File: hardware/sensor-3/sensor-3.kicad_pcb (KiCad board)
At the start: 2 copper layers, 11 x 32 mm, 12 parts, among them J101 2x05_Horizontal, U101 A31010SEHALT-10

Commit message: Update sensors
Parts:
- C101: footprint Capacitor_SMD:C_0603_1608Metric -> V2_Capacitor_SMD:C_0603
- FID101, FID102: value Fiducial -> Fiducial_Paste
- INFO101: value ORDER-NUMBER -> Order_Number
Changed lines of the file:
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@@
 			)
 		)
-		(property "Value" "Fiducial"
+		(property "Value" "Fiducial_Paste"
 			(at 0 1.5 0)
 			(layer "F.Fab")
@@
 			(end -3.175 -1.2)
 			(stroke
-				(width 0.127)
-				(type solid)
-			)
-			(layer "F.SilkS")
-		)
-		(fp_line
-			(start 3.175 -3.7)
-			(end 3.175 -1.2)
-			(stroke
-				(width 0.127)
+				(width 0.1)
 				(type solid)
 			)
@@
 			(end 3.175 -3.7)
 			(stroke
-				(width 0.127)
+				(width 0.1)
 				(type solid)
 			)
@@
 			(end 2.54 -3.7)
 			(stroke
-				(width 0.127)
+				(width 0.1)
 				(type solid)
 			)
@@
 			(end -1.27 -3.7)
 			(stroke
-				(width 0.127)
-				(type solid)
-			)
-			(layer "F.SilkS")
-		)
-		(fp_line
-			(start -3.175 -1.2)
-			(end -3.175 -3.7)
-			(stroke
-				(width 0.127)
+				(width 0.1)
 				(type solid)
 			)
@@
 			(end -2.54 -3.7)
 			(stroke
-				(width 0.127)
-				(type solid)
-			)
+				(width 0.1)
+				(type solid)
+			)
+			(layer "F.SilkS")
+		)
+		(fp_poly
+			(pts
+				(xy 4.01 0.155) (xy 3.77 -0.175) (xy 4.25 -0.175) (xy 4.01 0.155)
+			)
+			(stroke
+				(width 0.12)
+				(type solid)
+			)
+			(fill yes)
 			(layer "F.SilkS")
 		)
@@
 			)
 			(layer "F.Fab")
+		)
+		(fp_text user "${REFERENCE}"
+			(at 0 -2.4 180)
+			(layer "F.Fab")
+			(effects
+				(font
+					(size 0.5 0.5)
+					(thickness 0.1)
+					(bold yes)
+				)
+			)
 		)
 		(pad "" smd roundrect
@@
 		)
 		(embedded_fonts no)
-		(model "../../3dmodels/V2_Connector_PinHeader_1.27mm.3dshapes/PinHeader_2x05_P1.27mm.stp"
+		(model "../../3dmodels/V2_Connector_PinHeader_1.27mm.3dshapes/PinHeader_2x05_P1.27mm_Horizontal.step"
 			(offset
 				(xyz 2.52 1.18 1.65)
@@
 			)
 		)
-		(property "Value" "Fiducial"
+		(property "Value" "Fiducial_Paste"
 			(at 0 1.5 0)
 			(layer "F.Fab")
@@
 		(embedded_fonts no)
 	)
-	(footprint "Capacitor_SMD:C_0603_1608Metric"
+	(footprint "V2_Capacitor_SMD:C_0603"
 		(layer "F.Cu")
 		(at 159.75 162.75)
@@
 		)
 		(fp_rect
-			(start -1.48 -0.73)
-			(end 1.48 0.73)
+			(start -1.23 -0.73)
+			(end 1.23 0.73)
 			(stroke
 				(width 0.05)
@@
 			(effects
 				(font
-					(size 0.4 0.4)
-					(thickness 0.06)
+					(size 0.3 0.3)
+					(thickness 0.05)
 				)
 			)
 		)
 		(pad "1" smd roundrect
-			(at -0.775 0)
-			(size 0.9 0.95)
+			(at -0.7 0)
+			(size 0.7 0.8)
 			(layers "F.Cu" "F.Mask" "F.Paste")
-			(roundrect_rratio 0.25)
+			(roundrect_rratio 0.1428571429)
 			(net 1 "+3V3")
 			(pintype "passive")
 		)
 		(pad "2" smd roundrect
-			(at 0.775 0)
-			(size 0.9 0.95)
+			(at 0.7 0)
+			(size 0.7 0.8)
 			(layers "F.Cu" "F.Mask" "F.Paste")
-			(roundrect_rratio 0.25)
+			(roundrect_rratio 0.1428571429)
 			(net 4 "GND")
 			(pintype "passive")
@@
 			)
 		)
-		(property "Value" "ORDER-NUMBER"
+		(property "Value" "Order_Number"
 			(at 0 2.27 90)
 			(unlocked yes)
@@
 		(embedded_fonts no)
 	)
-	(gr_arc
-		(start 165.25 179)
-		(mid 164.957107 179.707107)
-		(end 164.25 180)
-		(stroke
-			(width 0.05)
-			(type solid)
-		)
-		(layer "Edge.Cuts")
-	)
 	(gr_line
 		(start 154.25 149)
 		(end 154.25 177.75)
-		(stroke
-			(width 0.05)
-			(type solid)
-		)
-		(layer "Edge.Cuts")
-	)
-	(gr_line
-		(start 155.25 180)
-		(end 156.5 180)
-		(stroke
-			(width 0.05)
-			(type solid)
-		)
-		(layer "Edge.Cuts")
-	)
-	(gr_line
-		(start 163 180)
-		(end 164.25 180)
 		(stroke
 			(width 0.05)
@@
 	)
 	(gr_arc
+		(start 155.25 180)
+		(mid 154.542893 179.707107)
+		(end 154.25 179)
+		(stroke
+			(width 0.05)
+			(type solid)
+		)
+		(layer "Edge.Cuts")
+	)
+	(gr_line
+		(start 155.25 180)
+		(end 156.5 180)
+		(stroke
+			(width 0.05)
+			(type solid)
+		)
+		(layer "Edge.Cuts")
+	)
+	(gr_line
+		(start 163 180)
+		(end 164.25 180)
+		(stroke
+			(width 0.05)
+			(type solid)
+		)
+		(layer "Edge.Cuts")
+	)
+	(gr_arc
 		(start 164.25 148)
 		(mid 164.957107 148.292893)
@@
 		(layer "Edge.Cuts")
 	)
-	(gr_arc
-		(start 155.25 180)
-		(mid 154.542893 179.707107)
-		(end 154.25 179)
-		(stroke
-			(width 0.05)
-			(type solid)
-		)
-		(layer "Edge.Cuts")
-	)
 	(gr_line
 		(start 165.25 149)
@@
 		(stroke
 			(width 0.05)
+			(type solid)
+		)
+		(layer "Edge.Cuts")
+	)
+	(gr_arc
+		(start 165.25 179)
+		(mid 164.957107 179.707107)
+		(end 164.25 180)
+		(stroke
+			(width 0.05)

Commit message: Replace Order_Number
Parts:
- H101, H107, H108: value MountingHole_2.5mm -> 2.5mm
- INFO101: value Order_Number -> ~; footprint V2_Production:Order_Number -> V2_Production:Revision
- moved INFO101 2.26 mm to (164.0, 169.8)
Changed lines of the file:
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@@
 	(paper "A4")
 	(title_block
-		(date "2023-07-17")
-		(rev "1")
+		(date "2026-02-13")
+		(rev "2026-02-13")
 	)
 	(layers
@@
 			)
 		)
-		(property "Value" "MountingHole_2.5mm"
+		(property "Value" "2.5mm"
 			(at 0 2.23 0)
 			(unlocked yes)
@@
 			)
 		)
-		(property "Value" "MountingHole_2.5mm"
+		(property "Value" "2.5mm"
 			(at 0 2.23 0)
 			(unlocked yes)
@@
 			)
 		)
+		(pad "" smd roundrect
+			(at -0.7 0)
+			(size 0.7 0.8)
+			(layers "F.Paste")
+			(roundrect_rratio 0.1428571429)
+			(chamfer_ratio 0.3)
+			(chamfer top_right bottom_right)
+		)
+		(pad "" smd roundrect
+			(at 0.7 0)
+			(size 0.7 0.8)
+			(layers "F.Paste")
+			(roundrect_rratio 0.1428571429)
+			(chamfer_ratio 0.3)
+			(chamfer top_left bottom_left)
+		)
 		(pad "1" smd roundrect
 			(at -0.7 0)
 			(size 0.7 0.8)
-			(layers "F.Cu" "F.Mask" "F.Paste")
+			(layers "F.Cu" "F.Mask")
 			(roundrect_rratio 0.1428571429)
 			(net 1 "+3V3")
@@
 			(at 0.7 0)
 			(size 0.7 0.8)
-			(layers "F.Cu" "F.Mask" "F.Paste")
+			(layers "F.Cu" "F.Mask")
 			(roundrect_rratio 0.1428571429)
 			(net 4 "GND")
@@
 		)
 		(embedded_fonts no)
-		(model "${KICAD9_3DMODEL_DIR}/Capacitor_SMD.3dshapes/C_0603_1608Metric.step"
+		(model "../../3dmodels/V2_Capacitor_SMD.3dshapes/C_0603_1608Metric.step"
 			(offset
 				(xyz 0 0 0)
@@
 		)
 	)
-	(footprint "V2_Production:Order_Number"
+	(footprint "V2_Production:Revision"
 		(layer "F.Cu")
-		(at 164.25 167.5 90)
+		(at 164 169.75 90)
 		(property "Reference" "INFO101"
 			(at 0 -1.77 90)
@@
 			)
 		)
-		(property "Value" "Order_Number"
+		(property "Value" "~"
 			(at 0 2.27 90)
 			(unlocked yes)
@@
 		(sheetname "/")
 		(sheetfile "sensor-3.kicad_sch")
-		(attr exclude_from_pos_files exclude_from_bom)
-		(fp_rect
-			(start -7 -0.75)
-			(end 7 0.75)
-			(stroke
-				(width 0.05)
-				(type default)
-			)
-			(fill no)
-			(layer "F.CrtYd")
-		)
-		(fp_text user "${Order-Number}"
+		(attr exclude_from_pos_files exclude_from_bom allow_missing_courtyard)
+		(fp_text user "${REVISION} (${ISSUE_DATE})"
 			(at 0 0 90)
 			(unlocked yes)
@@
 			(effects
 				(font
-					(size 0.8 0.8)
-					(thickness 0.12)
+					(size 0.75 0.75)
+					(thickness 0.1)
+				)
+			)
+		)
+		(fp_text user "${REVISION} (${ISSUE_DATE})"
+			(at 0 0 90)
+			(unlocked yes)
+			(layer "F.Fab")
+			(effects
+				(font
+					(size 0.75 0.75)
+					(thickness 0.1)
 				)
 			)
@@
 		)
 		(embedded_fonts no)
-		(model "/Users/kay/Documents/KiCad/8.0/versioduo.kicad/3dmodels/V2_Sensor_Hall.3dshapes/A31010SEHALT-10.stp"
+		(model "../../3dmodels/V2_Sensor_Hall.3dshapes/A31010SEHALT-10.stp"
 			(offset
 				(xyz 0 0 0)
@@
 			)
 		)
-		(property "Value" "MountingHole_2.5mm"
+		(property "Value" "2.5mm"
 			(at 0 2.23 0)
 			(unlocked yes)

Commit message: Export stencil
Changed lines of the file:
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@@
 	(paper "A4")
 	(title_block
-		(date "2026-02-13")
+		(date "2026-02-25")
 		(rev "2026-02-13")
 	)
@@
 			)
 		)
+		(property "Mouser" "649-200211120001T4LF"
+			(at 0 0 180)
+			(unlocked yes)
+			(layer "F.Fab")
+			(hide yes)
+			(effects
+				(font
+					(size 1 1)
+					(thickness 0.15)
+				)
+			)
+		)
+		(property "Manufacturer" "Amphenol FCI"
+			(at 0 0 180)
+			(unlocked yes)
+			(layer "F.Fab")
+			(hide yes)
+			(effects
+				(font
+					(size 1 1)
+					(thickness 0.15)
+				)
+			)
+		)
+		(property "Product" "20021112-00010T4LF"
+			(at 0 0 180)
+			(unlocked yes)
+			(layer "F.Fab")
+			(hide yes)
+			(effects
+				(font
+					(size 1 1)
+					(thickness 0.15)
+				)
+			)
+		)
 		(sheetname "/")
 		(sheetfile "sensor-3.kicad_sch")
@@
 			)
 		)
+		(property "Mouser" "810-CGA3E2X7R1H104MA"
+			(at 0 0 0)
+			(unlocked yes)
+			(layer "F.Fab")
+			(hide yes)
+			(effects
+				(font
+					(size 1 1)
+					(thickness 0.15)
+				)
+			)
+		)
+		(property "Manufacturer" "TDK"
+			(at 0 0 0)
+			(unlocked yes)
+			(layer "F.Fab")
+			(hide yes)
+			(effects
+				(font
+					(size 1 1)
+					(thickness 0.15)
+				)
+			)
+		)
+		(property "Product" "CGA3E2X7R1H104M080AA"
+			(at 0 0 0)
+			(unlocked yes)
+			(layer "F.Fab")
+			(hide yes)
+			(effects
+				(font
+					(size 1 1)
+					(thickness 0.15)
+				)
+			)
+		)
+		(property "Rating" "50V"
+			(at 0 0 0)
+			(unlocked yes)
+			(layer "F.Fab")
+			(hide yes)
+			(effects
+				(font
+					(size 1 1)
+					(thickness 0.15)
+				)
+			)
+		)
 		(property ki_fp_filters "C_*")
 		(sheetname "/")
@@
 				(font
 					(size 1.27 1.27)
+					(thickness 0.15)
+				)
+			)
+		)
+		(property "Manufacturer" "Allegro MicroSystems"
+			(at 0 0 0)
+			(unlocked yes)
+			(layer "F.Fab")
+			(hide yes)
+			(effects
+				(font
+					(size 1 1)
+					(thickness 0.15)
+				)
+			)
+		)
+		(property "Product" "A31010SEHALT-10"
+			(at 0 0 0)
+			(unlocked yes)
+			(layer "F.Fab")
+			(hide yes)
+			(effects
+				(font
+					(size 1 1)
+					(thickness 0.15)
+				)
+			)
+		)
+		(property "Mouser" "250-A31010SEHALT-10"
+			(at 0 0 0)
+			(unlocked yes)
+			(layer "F.Fab")
+			(hide yes)
+			(effects
+				(font
+					(size 1 1)
 					(thickness 0.15)
 				)
@@
 			)
 		)
+		(property "Sim.Enable" "0"
+			(at 0 0 90)
+			(unlocked yes)
+			(layer "F.Fab")
+			(hide yes)
+			(effects
+				(font
+					(size 1 1)
+					(thickness 0.15)
+				)
+			)
+		)
 		(sheetname "/")
 		(sheetfile "sensor-3.kicad_sch")
@@
 					(thickness 0.15)
 				)
+			)
+		)
+		(property "Sim.Enable" "0"
+			(at 0 0 180)
+			(unlocked yes)
+			(layer "F.Fab")
+			(hide yes)
+			(effects
+				(font
+					(size 1 1)
+					(thickness 0.15)
+				)

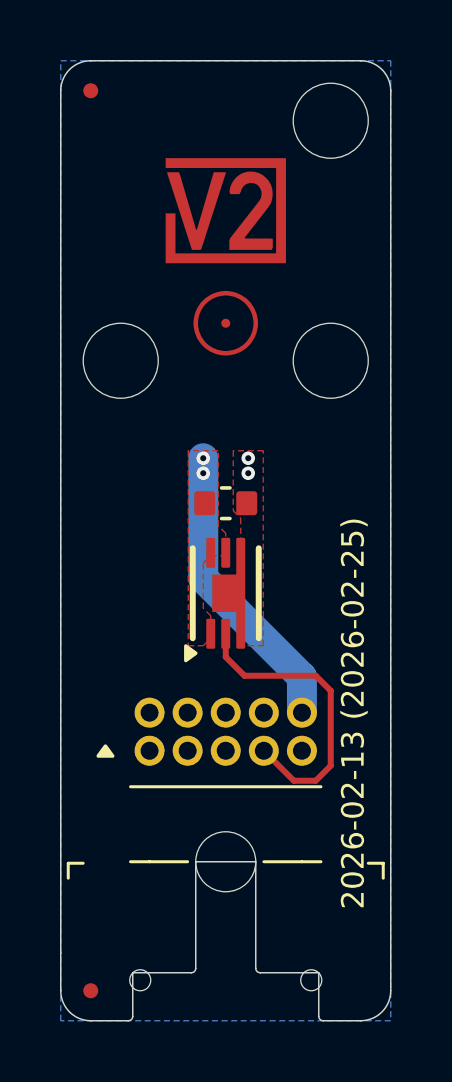
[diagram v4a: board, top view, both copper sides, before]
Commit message: KiCad 10
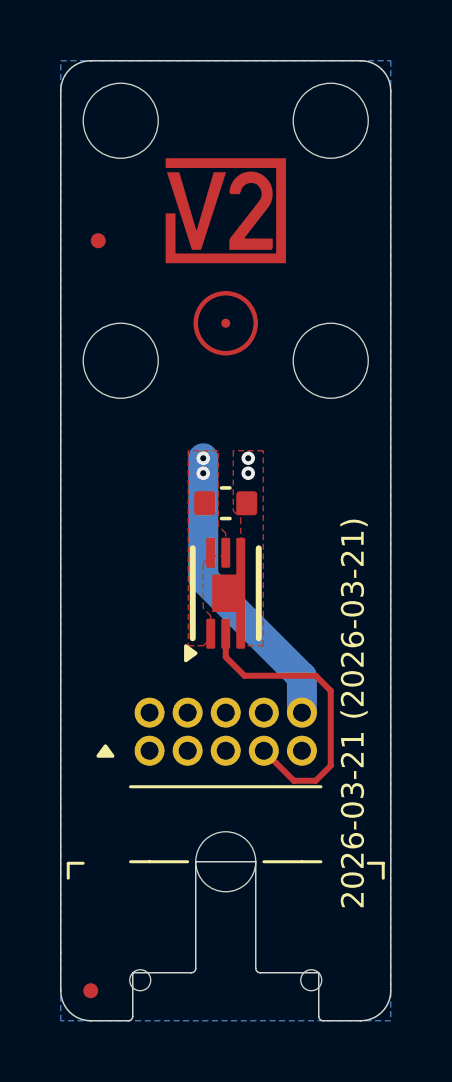
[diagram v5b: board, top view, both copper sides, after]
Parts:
- added H102: 2.5mm, V2_Mechanical:MountingHole_2.5mm, F.Cu at (156.2, 150.0)
- moved FID102 5.01 mm to (155.5, 154.0)
